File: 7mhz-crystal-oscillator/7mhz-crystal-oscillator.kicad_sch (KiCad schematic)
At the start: 12 parts, among them J1 Conn_Coaxial, Q1 2N3904, Y1 7MHz

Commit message: 7mhz xtal oscillator
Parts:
- added C4: .1u, symbol Device:C_Small
- added SW1: SW_SPST, symbol Switch:SW_SPST
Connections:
- net at Q1.3 (C), R4.2: now also C4.1; no longer J1.1 (In)
- net at R1.1: now also SW1.2 (B); no longer BT1.1 (+)
- new net: C4.2, J1.1 (In)
- new net: BT1.1 (+), SW1.1 (A)
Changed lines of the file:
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@@
     (stroke (width 0) (type default))
   )
-  (wire (pts (xy 64.77 67.31) (xy 48.26 67.31))
+  (wire (pts (xy 64.77 67.31) (xy 60.96 67.31))
     (stroke (width 0) (type default))
   )
@@
     (stroke (width 0) (type default))
   )
+  (wire (pts (xy 50.8 67.31) (xy 48.26 67.31))
+    (stroke (width 0) (type default))
+  )
   (wire (pts (xy 118.11 91.44) (xy 118.11 93.98))
     (stroke (width 0) (type default))
   )
-  (wire (pts (xy 97.79 86.36) (xy 113.03 86.36))
+  (wire (pts (xy 97.79 86.36) (xy 101.6 86.36))
     (stroke (width 0) (type default))
   )
@@
     (stroke (width 0) (type default))
   )
+  (wire (pts (xy 106.68 86.36) (xy 113.03 86.36))
+    (stroke (width 0) (type default))
+  )
   (wire (pts (xy 109.22 69.85) (xy 109.22 67.31))
     (stroke (width 0) (type default))
@@
         (path "/0b54bfea-3162-44d0-afdf-898cf06ebb22"
           (reference "#PWR01") (unit 1)
+        )
+      )
+    )
+  )
+  (symbol (lib_id "Device:C_Small") (at 104.14 86.36 90) (unit 1)
+    (in_bom yes) (on_board yes) (dnp no) (fields_autoplaced)
+    (property "Reference" "C4" (at 104.1463 80.01 90)
+      (effects (font (size 1.27 1.27)))
+    )
+    (property "Value" ".1u" (at 104.1463 82.55 90)
+      (effects (font (size 1.27 1.27)))
+    )
+    (property "Footprint" "" (at 104.14 86.36 0)
+      (effects (font (size 1.27 1.27)) hide)
+    )
+    (property "Datasheet" "~" (at 104.14 86.36 0)
+      (effects (font (size 1.27 1.27)) hide)
+    )
+    (pin "1")
+    (pin "2")
+    (instances
+      (project "7mhz-crystal-oscillator"
+        (path "/0b54bfea-3162-44d0-afdf-898cf06ebb22"
+          (reference "C4") (unit 1)
         )
       )
@@
         )
       )
+    )
+  )
+  (symbol (lib_id "Switch:SW_SPST") (at 55.88 67.31 0) (unit 1)
+    (in_bom yes) (on_board yes) (dnp no) (fields_autoplaced)
+    (property "Reference" "SW1" (at 55.88 60.96 0)
+      (effects (font (size 1.27 1.27)))
+    )
+    (property "Value" "SW_SPST" (at 55.88 63.5 0)
+      (effects (font (size 1.27 1.27)))
+    )
+    (property "Footprint" "" (at 55.88 67.31 0)
+      (effects (font (size 1.27 1.27)) hide)
+    )
+    (property "Datasheet" "~" (at 55.88 67.31 0)
+      (effects (font (size 1.27 1.27)) hide)
+    )
+    (pin "2")
+    (pin "1")
+    (instances
+      (project "7mhz-crystal-oscillator"
+        (path "/0b54bfea-3162-44d0-afdf-898cf06ebb22"
+          (reference "SW1") (unit 1)
+        )
+      )

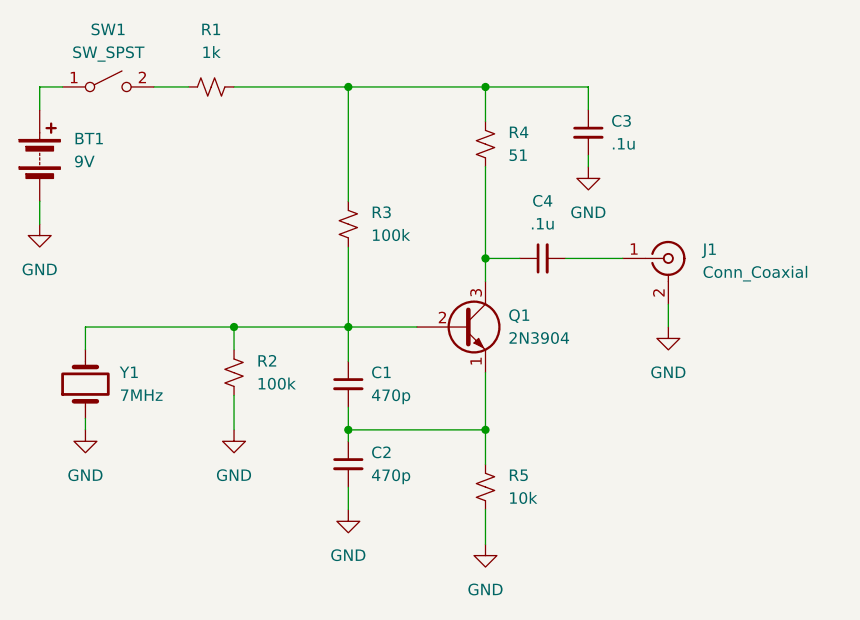
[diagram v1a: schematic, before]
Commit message: crystal oscillator models
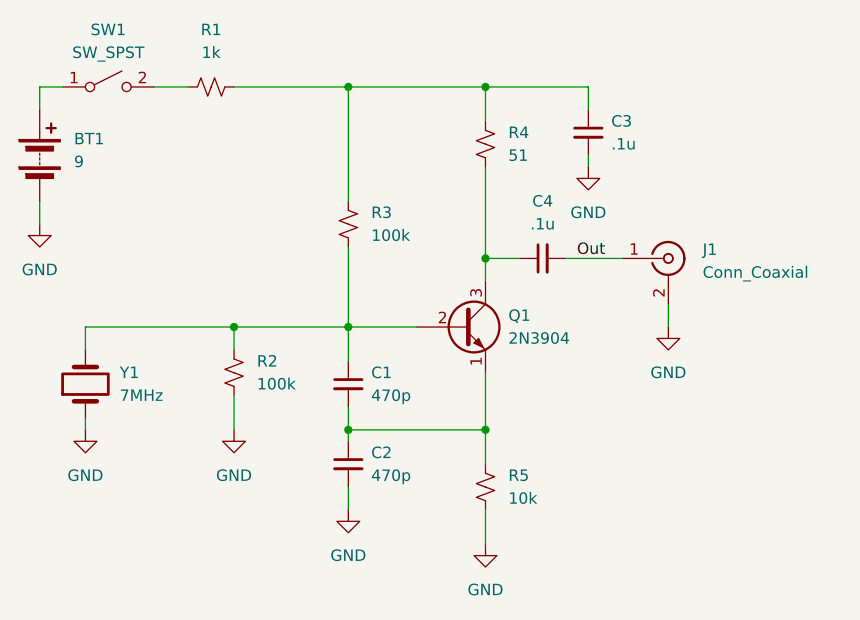
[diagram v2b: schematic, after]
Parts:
- BT1: value 9V -> 9
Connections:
- net Out: now reaches C4.2, J1.1 (In)
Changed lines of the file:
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@@
     (stroke (width 0) (type default))
+  )
+  (label "Out" (at 107.95 86.36 0) (fields_autoplaced)
+    (effects (font (size 1.27 1.27)) (justify left bottom))
   )
   (symbol (lib_id "Device:C_Small") (at 109.22 72.39 0) (unit 1)
@@
     )
     (property "Datasheet" "~" (at 53.34 100.33 0)
+      (effects (font (size 1.27 1.27)) hide)
+    )
+    (property "Sim.Library" "xtal.lib" (at 53.34 100.33 0)
+      (effects (font (size 1.27 1.27)) hide)
+    )
+    (property "Sim.Name" "vdivide" (at 53.34 100.33 0)
+      (effects (font (size 1.27 1.27)) hide)
+    )
+    (property "Sim.Device" "SUBCKT" (at 53.34 100.33 0)
+      (effects (font (size 1.27 1.27)) hide)
+    )
+    (property "Sim.Pins" "1=1 2=2" (at 53.34 100.33 0)
       (effects (font (size 1.27 1.27)) hide)
     )
@@
       (effects (font (size 1.27 1.27)) (justify left) hide)
     )
+    (property "Sim.Device" "NPN" (at 95.25 93.98 0)
+      (effects (font (size 1.27 1.27)) hide)
+    )
+    (property "Sim.Type" "VBIC" (at 95.25 93.98 0)
+      (effects (font (size 1.27 1.27)) hide)
+    )
+    (property "Sim.Pins" "1=E 2=B 3=C" (at 95.25 93.98 0)
+      (effects (font (size 1.27 1.27)) hide)
+    )
     (pin "3")
     (pin "1")
@@
       (effects (font (size 1.27 1.27)) (justify left))
     )
-    (property "Value" "9V" (at 52.07 75.6285 0)
+    (property "Value" "9" (at 52.07 75.6285 0)
       (effects (font (size 1.27 1.27)) (justify left))
     )
@@
       (effects (font (size 1.27 1.27)) hide)
     )
+    (property "Sim.Device" "V" (at 48.26 74.93 0)
+      (effects (font (size 1.27 1.27)) hide)
+    )
+    (property "Sim.Type" "DC" (at 48.26 74.93 0)
+      (effects (font (size 1.27 1.27)) hide)
+    )
+    (property "Sim.Pins" "1=+ 2=-" (at 48.26 74.93 0)
+      (effects (font (size 1.27 1.27)) hide)
+    )
     (pin "2")
     (pin "1")
@@
       (effects (font (size 1.27 1.27)) hide)
     )
+    (property "Sim.Enable" "0" (at 55.88 67.31 0)
+      (effects (font (size 1.27 1.27)) hide)
+    )
     (pin "2")
     (pin "1")
@@
       (effects (font (size 1.27 1.27)) hide)
     )
+    (property "Sim.Enable" "0" (at 118.11 86.36 0)
+      (effects (font (size 1.27 1.27)) hide)
+    )
